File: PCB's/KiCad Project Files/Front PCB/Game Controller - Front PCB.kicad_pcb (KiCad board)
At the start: 2 copper layers, 70 x 65 mm, 54 parts, among them M1_N1 MOSI, M1_P1 MOSI, M2_N1 MOSI, M2_P1 MOSI, Q1 2N7002, Q2 2N7002, SW1 A, SW2 B, SW3 X, SW4 Y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

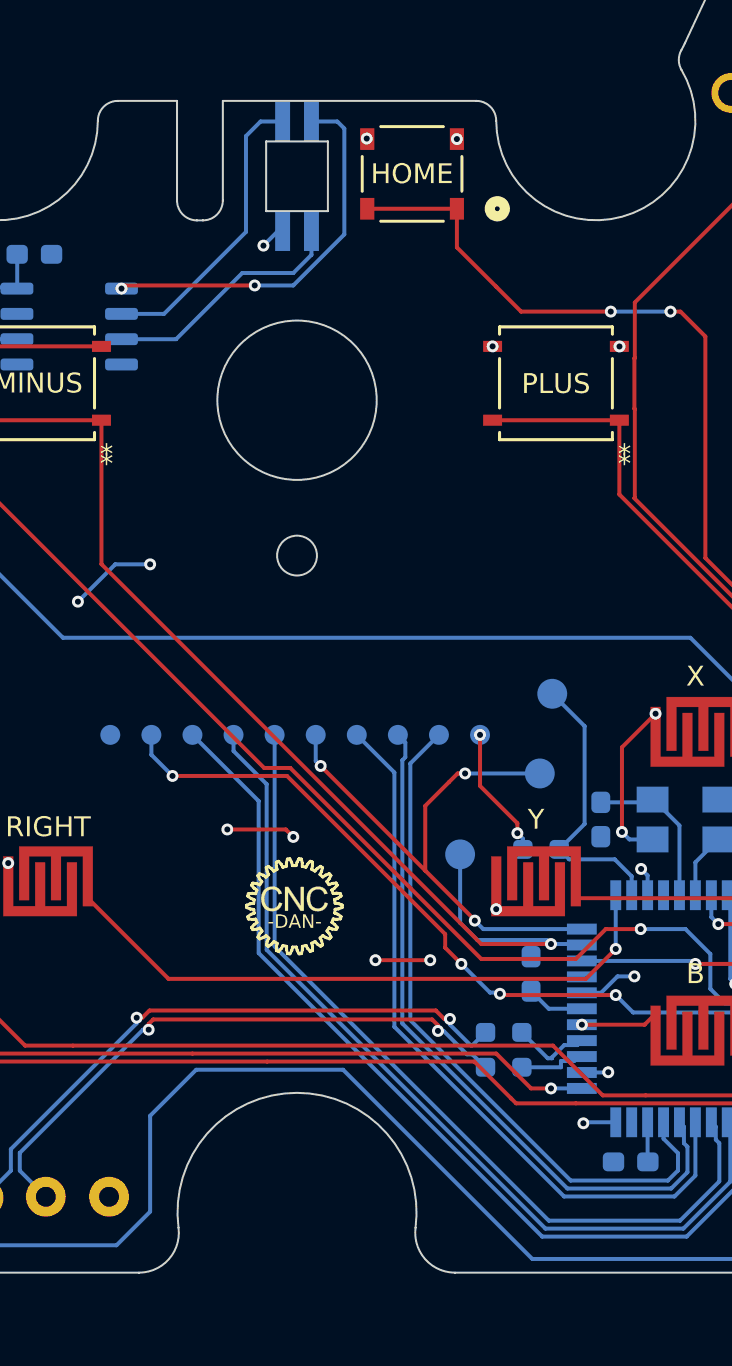
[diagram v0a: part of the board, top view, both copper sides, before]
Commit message: Updated front PCB drawing and kicad project files
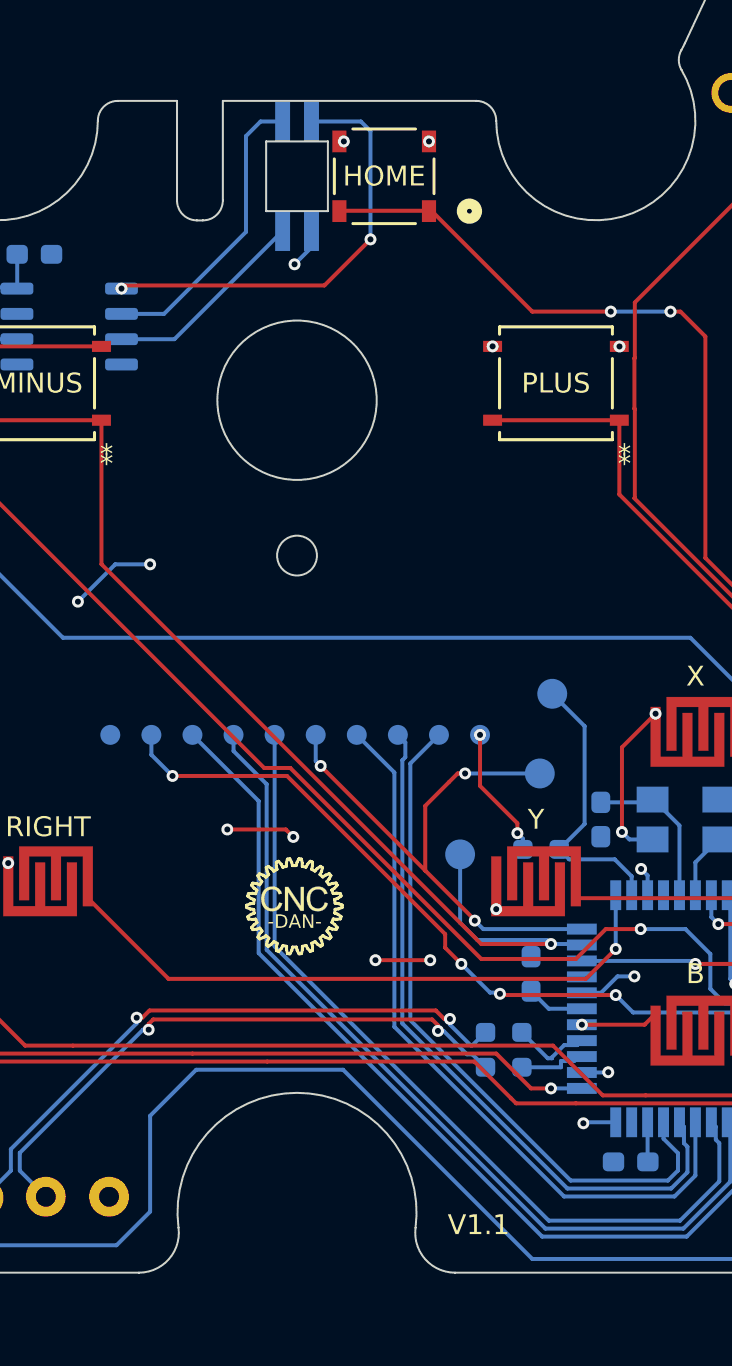
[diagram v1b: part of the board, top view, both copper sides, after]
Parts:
- moved SW9 1.41 mm to (157.4, 77.7)
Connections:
- D1 pad 1: Net-(D1-BA) -> VCC
- D1 pad 4: VCC -> Net-(D1-K)
- U7 pad 3: Net-(D1-BA) -> Net-(D1-K)
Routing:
- net Net-(D1-BA): track 12.5 -> 0.00 mm
- net Net-(D1-K): track 0.00 -> 10.3 mm
- net Net-(D1-RA): track 19.4 -> 22.1 mm
- net VCC: track 25.5 -> 26.2 mm
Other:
- board text added: "V1.1"
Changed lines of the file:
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@@
 	(net 40 "Net-(U7-DIN)")
 	(net 41 "Net-(D1-GA)")
-	(net 42 "Net-(D1-BA)")
+	(net 42 "Net-(D1-K)")
 	(net 43 "unconnected-(U7-SET-Pad7)")
 	(net 44 "Net-(D1-RA)")
@@
 			)
 		)
-		(fp_text user "*"
-			(at -2.3241 -2.6289 180)
+		(fp_text user "${REFERENCE}"
+			(at 0 0 180)
+			(unlocked yes)
 			(layer "F.Fab")
 			(effects
@@
 			)
 		)
-		(fp_text user "${REFERENCE}"
-			(at 0 0 180)
-			(unlocked yes)
+		(fp_text user "*"
+			(at -2.3241 -2.6289 180)
 			(layer "F.Fab")
 			(effects
@@
 	(footprint "Parts:TL3315NF100Q_EWI"
 		(layer "F.Cu")
-		(at 158.774999 77.587712 180)
+		(at 157.375 77.706356 180)
 		(tags "TL3315NF100Q ")
 		(property "Reference" "SW9"
@@
 		)
 		(property "Value" "PLUS"
-			(at 0 -0.025 0)
+			(at 0 0 0)
 			(unlocked yes)
 			(layer "F.SilkS")
@@
 		(fp_text user "*"
 			(at -3.43535 -3.556 180)
+			(unlocked yes)
 			(layer "F.SilkS")
 			(effects
@@
 		(fp_text user "*"
 			(at -3.43535 -3.556 180)
-			(unlocked yes)
 			(layer "F.SilkS")
 			(effects
@@
 			)
 		)
-		(fp_text user "${REFERENCE}"
-			(at 0 0 180)
-			(unlocked yes)
+		(fp_text user "*"
+			(at -2.3241 -2.6289 180)
 			(layer "F.Fab")
 			(effects
@@
 		(fp_text user "*"
 			(at -2.3241 -2.6289 180)
+			(unlocked yes)
 			(layer "F.Fab")
 			(effects
@@
 			)
 		)
-		(fp_text user "*"
-			(at -2.3241 -2.6289 180)
+		(fp_text user "${REFERENCE}"
+			(at 0 0 180)
 			(unlocked yes)
 			(layer "F.Fab")
@@
 			(layers "B.Cu" "B.Paste" "B.Mask")
 			(roundrect_rratio 0.25)
-			(net 42 "Net-(D1-BA)")
+			(net 42 "Net-(D1-K)")
 			(pinfunction "OUTB")
 			(pintype "output")
@@
 		(attr smd)
 		(fp_circle
-			(center -4.5 1.075)
-			(end -4.4 1.075)
+			(center -4.5 -1)
+			(end -4.4 -1)
 			(stroke
 				(width 0.2)
@@
 		)
 		(fp_circle
-			(center -4.5 1.075)
-			(end -4.4 1.075)
+			(center -4.5 -1)
+			(end -4.4 -1)
 			(stroke
 				(width 0.2)
@@
 			(size 2 0.75)
 			(layers "B.Cu" "B.Paste" "B.Mask")
-			(net 42 "Net-(D1-BA)")
+			(net 2 "VCC")
 			(pinfunction "BA")
 			(pintype "passive")
@@
 			(size 2 0.75)
 			(layers "B.Cu" "B.Paste" "B.Mask")
-			(net 2 "VCC")
+			(net 42 "Net-(D1-K)")
 			(pinfunction "K")
 			(pintype "passive")
@@
 		)
 	)
+	(gr_text "V1.1"
+		(at 160.5625 130.9375 0)
+		(layer "F.SilkS")
+		(effects
+			(font
+				(size 1 1)
+				(thickness 0.1)
+			)
+			(justify left bottom)
+		)
+	)
 	(segment
 		(start 143.18135 86.2458)
@@
 	)
 	(via
-		(at 161.025 75.83771)
+		(at 159.625001 75.956354)
 		(size 0.6)
 		(drill 0.3)
@@
 	)
 	(via
-		(at 156.5 75.8125)
+		(at 155.349999 75.956353)
 		(size 0.6)
 		(drill 0.3)
@@
 	)
 	(via
-		(at 151.3125 81.1875)
-		(size 0.6)
-		(drill 0.3)
-		(layers "F.Cu" "B.Cu")
-		(net 2)
-	)
-	(via
 		(at 142 99.0625)
 		(size 0.6)
@@
 	)
 	(via
+		(at 152.875 82.125)
+		(size 0.6)
+		(drill 0.3)
+		(layers "F.Cu" "B.Cu")
+		(net 2)
+	)
+	(via
 		(at 136.625 81.4375)
 		(size 0.6)
@@
 	)
 	(segment
+		(start 153.724999 80.456356)
+		(end 153.724999 81.275001)
+		(width 0.2)
+		(layer "B.Cu")
+		(net 2)
+	)
+	(segment
 		(start 145.625 97.1875)
 		(end 143.875 97.1875)
@@
 	)
 	(segment
-		(start 152.274999 80.456356)
-		(end 152.043644 80.456356)
+		(start 153.724999 81.275001)
+		(end 152.875 82.125)
 		(width 0.2)
 		(layer "B.Cu")
@@
 	)
 	(segment
-		(start 152.043644 80.456356)
-		(end 151.3125 81.1875)
-		(width 0.2)
-		(layer "B.Cu")
-		(net 2)
-	)
-	(segment
 		(start 177 126.4375)
 		(end 177.5 126.9375)
@@
 	)
 	(segment
-		(start 163 83.25)
-		(end 164.25 84.5)
+		(start 155.274997 79.4375)
+		(end 155.149999 79.312502)
 		(width 0.2)
 		(layer "F.Cu")
@@
 	)
 	(segment
-		(start 173.5 85.75)
-		(end 173.5 96.868628)
+		(start 164.812499 84.5)
+		(end 159.749999 79.4375)
 		(width 0.2)
 		(layer "F.Cu")
@@
 	)
 	(segment
-		(start 164.25 84.5)
-		(end 168.75 84.5)
+		(start 173.5 85.75)
+		(end 173.5 96.868628)
 		(width 0.2)
 		(layer "F.Cu")
@@
 	)
 	(segment
-		(start 161.025 81.275)
-		(end 163 83.25)
+		(start 168.75 84.5)
+		(end 164.812499 84.5)
 		(width 0.2)
 		(layer "F.Cu")
@@
 	)
 	(segment
-		(start 156.524998 79.337714)
-		(end 161.025 79.337714)
+		(start 159.749999 79.4375)
+		(end 155.274997 79.4375)
 		(width 0.2)
 		(layer "F.Cu")
@@
 	)
 	(segment
-		(start 161.025 79.337714)
-		(end 161.025 81.275)
-		(width 0.2)
-		(layer "F.Cu")
-		(net 27)
-	)
-	(segment
 		(start 186.5 109.868628)
 		(end 186.5 114.565686)
@@
 	)
 	(segment
-		(start 153.724999 80.456356)
-		(end 153.724999 81.650001)
-		(width 0.2)
-		(layer "B.Cu")
-		(net 42)
-	)
-	(segment
-		(start 150.25 82.5625)
-		(end 146.9275 85.885)
-		(width 0.2)
-		(layer "B.Cu")
-		(net 42)
-	)
-	(segment
-		(start 146.9275 85.885)
+		(start 146.846355 85.885)
 		(end 144.1875 85.885)
 		(width 0.2)
@@
 	)
 	(segment
-		(start 153.724999 81.650001)
-		(end 152.8125 82.5625)
-		(width 0.2)
-		(layer "B.Cu")
-		(net 42)
-	)
-	(segment
-		(start 152.8125 82.5625)
-		(end 150.25 82.5625)
+		(start 152.274999 80.456356)
+		(end 146.846355 85.885)
 		(width 0.2)
 		(layer "B.Cu")
@@
 	)
 	(segment
-		(start 150.875 83.1875)
+		(start 154.375 83.1875)
 		(end 144.345 83.1875)
 		(width 0.2)
@@
 		(net 44)
 	)
+	(segment
+		(start 156.6875 80.875)
+		(end 154.375 83.1875)
+		(width 0.2)
+		(layer "F.Cu")
+		(net 44)
+	)
 	(via
-		(at 150.875 83.1875)
+		(at 156.6875 80.875)
 		(size 0.6)
 		(drill 0.3)
@@
 	)
 	(segment
-		(start 153.724999 74.956356)
-		(end 155.021192 74.956356)
-		(width 0.2)
-		(layer "B.Cu")
-		(net 44)
-	)
-	(segment
-		(start 152.8125 83.1875)
-		(end 150.875 83.1875)
-		(width 0.2)
-		(layer "B.Cu")
-		(net 44)
-	)
-	(segment
-		(start 155.375 80.625)
-		(end 152.8125 83.1875)
+		(start 156.206356 74.956356)
+		(end 153.724999 74.956356)
 		(width 0.2)
 		(layer "B.Cu")
@@
 	)
 	(segment
-		(start 155.375 75.310164)
-		(end 155.375 80.625)
+		(start 156.6875 75.4375)
+		(end 156.206356 74.956356)
 		(width 0.2)
 		(layer "B.Cu")
@@
 	)
 	(segment
-		(start 155.021192 74.956356)
-		(end 155.375 75.310164)
+		(start 156.6875 80.875)
+		(end 156.6875 75.4375)
 		(width 0.2)
 		(layer "B.Cu")
